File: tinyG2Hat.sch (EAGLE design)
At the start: 31 parts

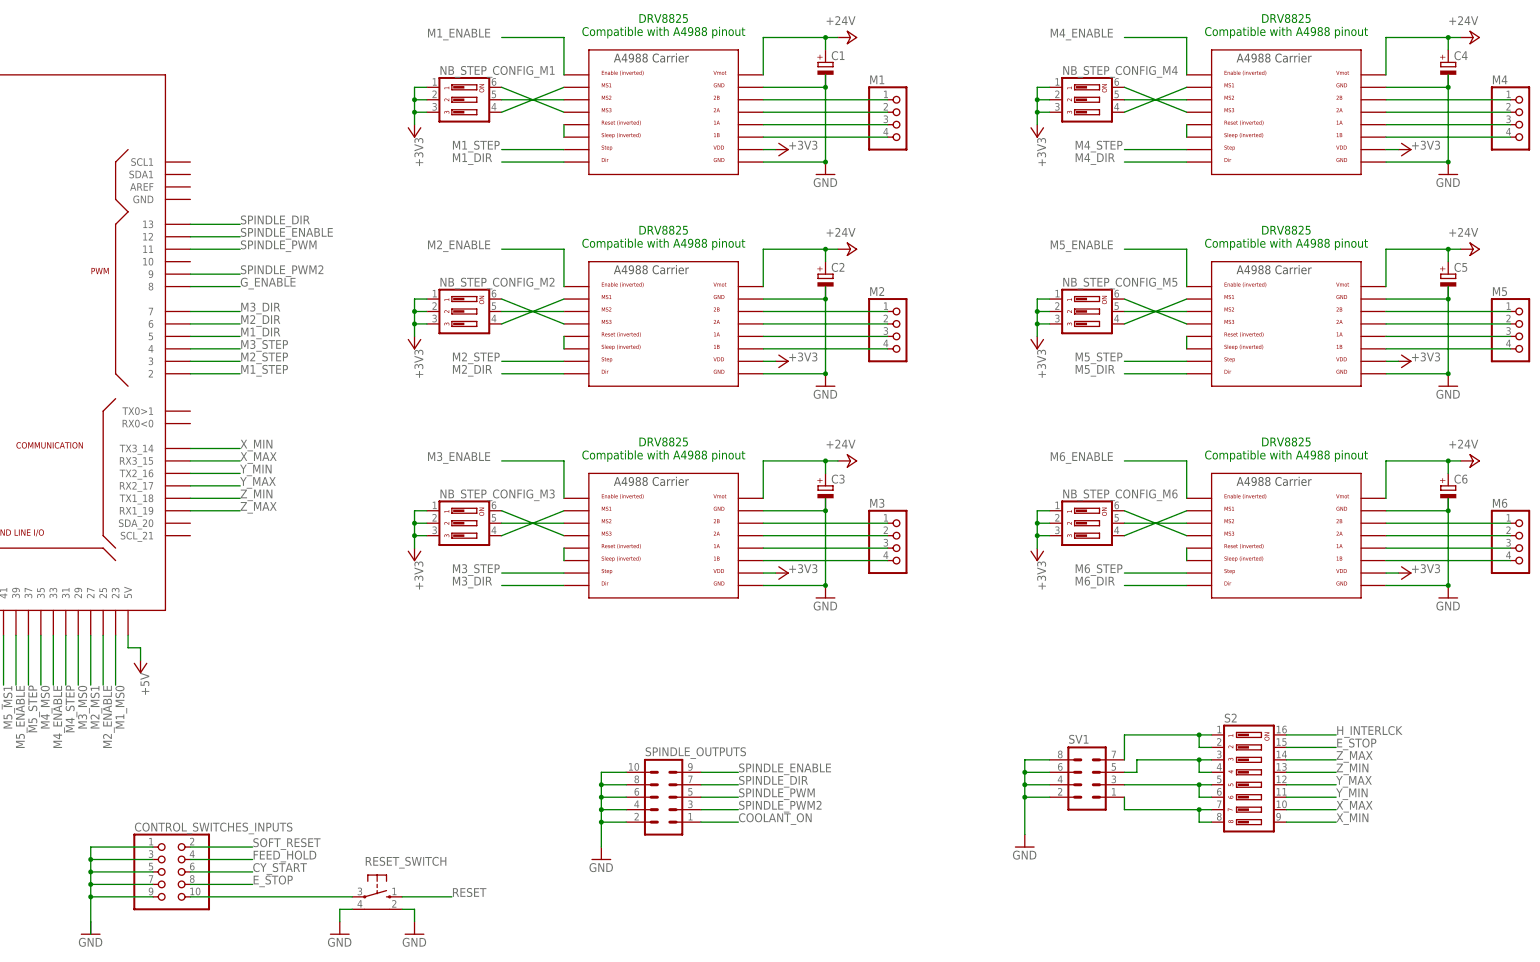
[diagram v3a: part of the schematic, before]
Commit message: Routage du Spindle, M1 et M2
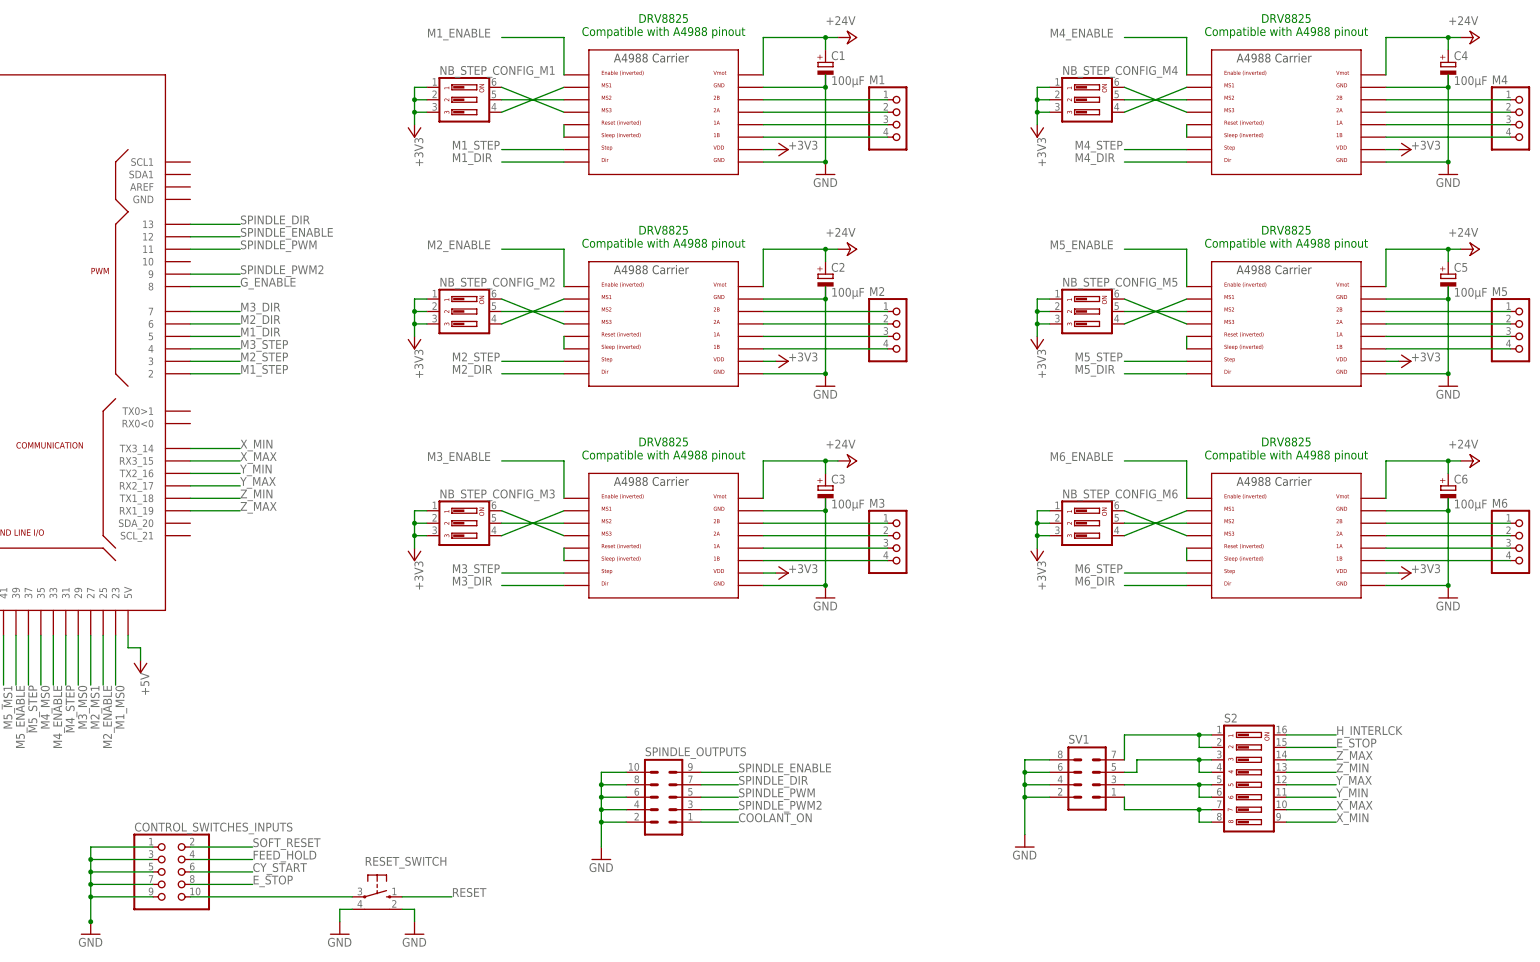
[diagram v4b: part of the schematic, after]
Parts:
- C1, C2, C3, C4, C5, C6: value (none) -> 100µF
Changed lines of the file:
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@@
 <part name="P+4" library="supply1" library_urn="urn:adsk.eagle:library:371" deviceset="+24V" device=""/>
 <part name="M1" library="pinhead" library_urn="urn:adsk.eagle:library:325" deviceset="PINHD-1X4" device="" package3d_urn="urn:adsk.eagle:package:22407/2"/>
-<part name="C1" library="rcl" library_urn="urn:adsk.eagle:library:334" deviceset="CPOL-EU" device="E3.5-8" package3d_urn="urn:adsk.eagle:package:23360/2"/>
+<part name="C1" library="rcl" library_urn="urn:adsk.eagle:library:334" deviceset="CPOL-EU" device="E3.5-8" package3d_urn="urn:adsk.eagle:package:23360/2" value="100µF"/>
 <part name="MOTOR_POWER" library="RepRapjr" deviceset="RAPC712" device="0"/>
 <part name="GND5" library="supply1" library_urn="urn:adsk.eagle:library:371" deviceset="GND" device=""/>
@@
 <part name="P+6" library="supply1" library_urn="urn:adsk.eagle:library:371" deviceset="+24V" device=""/>
 <part name="M2" library="pinhead" library_urn="urn:adsk.eagle:library:325" deviceset="PINHD-1X4" device="" package3d_urn="urn:adsk.eagle:package:22407/2"/>
-<part name="C2" library="rcl" library_urn="urn:adsk.eagle:library:334" deviceset="CPOL-EU" device="E3.5-8" package3d_urn="urn:adsk.eagle:package:23360/2"/>
+<part name="C2" library="rcl" library_urn="urn:adsk.eagle:library:334" deviceset="CPOL-EU" device="E3.5-8" package3d_urn="urn:adsk.eagle:package:23360/2" value="100µF"/>
 <part name="U$3" library="RepRapjr" deviceset="A4988BREAKOUT" device=""/>
 <part name="GND7" library="supply1" library_urn="urn:adsk.eagle:library:371" deviceset="GND" device=""/>
@@
 <part name="P+7" library="supply1" library_urn="urn:adsk.eagle:library:371" deviceset="+24V" device=""/>
 <part name="M3" library="pinhead" library_urn="urn:adsk.eagle:library:325" deviceset="PINHD-1X4" device="" package3d_urn="urn:adsk.eagle:package:22407/2"/>
-<part name="C3" library="rcl" library_urn="urn:adsk.eagle:library:334" deviceset="CPOL-EU" device="E3.5-8" package3d_urn="urn:adsk.eagle:package:23360/2"/>
+<part name="C3" library="rcl" library_urn="urn:adsk.eagle:library:334" deviceset="CPOL-EU" device="E3.5-8" package3d_urn="urn:adsk.eagle:package:23360/2" value="100µF"/>
 <part name="U$4" library="RepRapjr" deviceset="A4988BREAKOUT" device=""/>
 <part name="GND8" library="supply1" library_urn="urn:adsk.eagle:library:371" deviceset="GND" device=""/>
@@
 <part name="P+8" library="supply1" library_urn="urn:adsk.eagle:library:371" deviceset="+24V" device=""/>
 <part name="M4" library="pinhead" library_urn="urn:adsk.eagle:library:325" deviceset="PINHD-1X4" device="" package3d_urn="urn:adsk.eagle:package:22407/2"/>
-<part name="C4" library="rcl" library_urn="urn:adsk.eagle:library:334" deviceset="CPOL-EU" device="E3.5-8" package3d_urn="urn:adsk.eagle:package:23360/2"/>
+<part name="C4" library="rcl" library_urn="urn:adsk.eagle:library:334" deviceset="CPOL-EU" device="E3.5-8" package3d_urn="urn:adsk.eagle:package:23360/2" value="100µF"/>
 <part name="U$5" library="RepRapjr" deviceset="A4988BREAKOUT" device=""/>
 <part name="GND9" library="supply1" library_urn="urn:adsk.eagle:library:371" deviceset="GND" device=""/>
@@
 <part name="P+9" library="supply1" library_urn="urn:adsk.eagle:library:371" deviceset="+24V" device=""/>
 <part name="M5" library="pinhead" library_urn="urn:adsk.eagle:library:325" deviceset="PINHD-1X4" device="" package3d_urn="urn:adsk.eagle:package:22407/2"/>
-<part name="C5" library="rcl" library_urn="urn:adsk.eagle:library:334" deviceset="CPOL-EU" device="E3.5-8" package3d_urn="urn:adsk.eagle:package:23360/2"/>
+<part name="C5" library="rcl" library_urn="urn:adsk.eagle:library:334" deviceset="CPOL-EU" device="E3.5-8" package3d_urn="urn:adsk.eagle:package:23360/2" value="100µF"/>
 <part name="U$6" library="RepRapjr" deviceset="A4988BREAKOUT" device=""/>
 <part name="GND10" library="supply1" library_urn="urn:adsk.eagle:library:371" deviceset="GND" device=""/>
@@
 <part name="P+10" library="supply1" library_urn="urn:adsk.eagle:library:371" deviceset="+24V" device=""/>
 <part name="M6" library="pinhead" library_urn="urn:adsk.eagle:library:325" deviceset="PINHD-1X4" device="" package3d_urn="urn:adsk.eagle:package:22407/2"/>
-<part name="C6" library="rcl" library_urn="urn:adsk.eagle:library:334" deviceset="CPOL-EU" device="E3.5-8" package3d_urn="urn:adsk.eagle:package:23360/2"/>
+<part name="C6" library="rcl" library_urn="urn:adsk.eagle:library:334" deviceset="CPOL-EU" device="E3.5-8" package3d_urn="urn:adsk.eagle:package:23360/2" value="100µF"/>
 <part name="SPINDLE_OUTPUTS" library="con-lstb" library_urn="urn:adsk.eagle:library:162" deviceset="MA05-2" device="" package3d_urn="urn:adsk.eagle:package:8329/1"/>
 <part name="GND11" library="supply1" library_urn="urn:adsk.eagle:library:371" deviceset="GND" device=""/>
@@
 </segment>
 <segment>
+<pinref part="RESET_SWITCH" gate="1" pin="GND2"/>
+<wire x1="203.2" y1="-30.48" x2="200.66" y2="-30.48" width="0.1524" layer="91"/>
+<pinref part="GND14" gate="1" pin="GND"/>
+<wire x1="200.66" y1="-30.48" x2="200.66" y2="-33.02" width="0.1524" layer="91"/>
+</segment>
+<segment>
+<pinref part="RESET_SWITCH" gate="1" pin="GND1"/>
+<wire x1="213.36" y1="-30.48" x2="215.9" y2="-30.48" width="0.1524" layer="91"/>
+<pinref part="GND15" gate="1" pin="GND"/>
+<wire x1="215.9" y1="-30.48" x2="215.9" y2="-33.02" width="0.1524" layer="91"/>
+</segment>
+<segment>
 <pinref part="CONTROL_SWITCHES_INPUTS" gate="A" pin="1"/>
 <wire x1="162.56" y1="-17.78" x2="149.86" y2="-17.78" width="0.1524" layer="91"/>
@@
 <wire x1="149.86" y1="-22.86" x2="149.86" y2="-25.4" width="0.1524" layer="91"/>
 <wire x1="149.86" y1="-25.4" x2="149.86" y2="-27.94" width="0.1524" layer="91"/>
-<wire x1="149.86" y1="-27.94" x2="149.86" y2="-33.02" width="0.1524" layer="91"/>
 <wire x1="162.56" y1="-20.32" x2="149.86" y2="-20.32" width="0.1524" layer="91"/>
 <junction x="149.86" y="-20.32"/>
@@
 <pinref part="CONTROL_SWITCHES_INPUTS" gate="A" pin="9"/>
 <wire x1="162.56" y1="-27.94" x2="149.86" y2="-27.94" width="0.1524" layer="91"/>
+<pinref part="GND13" gate="1" pin="GND"/>
+<wire x1="149.86" y1="-33.02" x2="149.86" y2="-27.94" width="0.1524" layer="91"/>
 <junction x="149.86" y="-27.94"/>
-<pinref part="GND13" gate="1" pin="GND"/>
-<wire x1="149.86" y1="-33.02" x2="149.86" y2="-35.56" width="0.1524" layer="91"/>
-</segment>
-<segment>
-<pinref part="RESET_SWITCH" gate="1" pin="GND2"/>
-<wire x1="203.2" y1="-30.48" x2="200.66" y2="-30.48" width="0.1524" layer="91"/>
-<pinref part="GND14" gate="1" pin="GND"/>
-<wire x1="200.66" y1="-30.48" x2="200.66" y2="-33.02" width="0.1524" layer="91"/>
-</segment>
-<segment>
-<pinref part="RESET_SWITCH" gate="1" pin="GND1"/>
-<wire x1="213.36" y1="-30.48" x2="215.9" y2="-30.48" width="0.1524" layer="91"/>
-<pinref part="GND15" gate="1" pin="GND"/>
-<wire x1="215.9" y1="-30.48" x2="215.9" y2="-33.02" width="0.1524" layer="91"/>
-</segment>
-</net>
+<junction x="149.86" y="-33.02"/>
+</segment>
+</net>
